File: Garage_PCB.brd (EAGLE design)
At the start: 35.6 x 44.4 mm, 19 parts, among them Q1 MOSFET-NCHANNELFQP30N06L

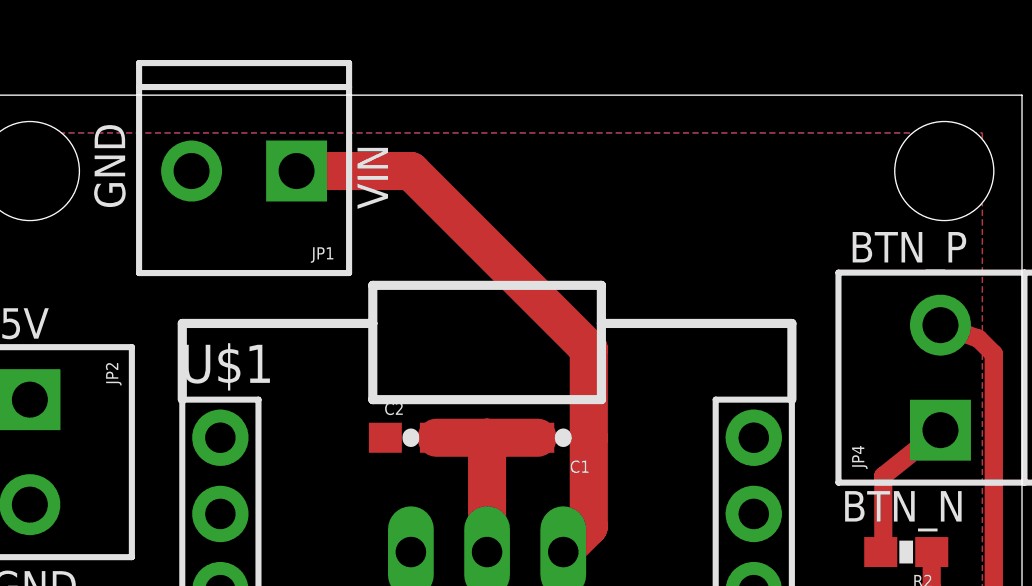
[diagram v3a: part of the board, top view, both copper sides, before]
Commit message: Added my name and the Spark logo
Added my name to the board and the Spark logo as well.  Also added the
Spark Eagle Library to the Eagle directory search paths so that I can
edit library parts.
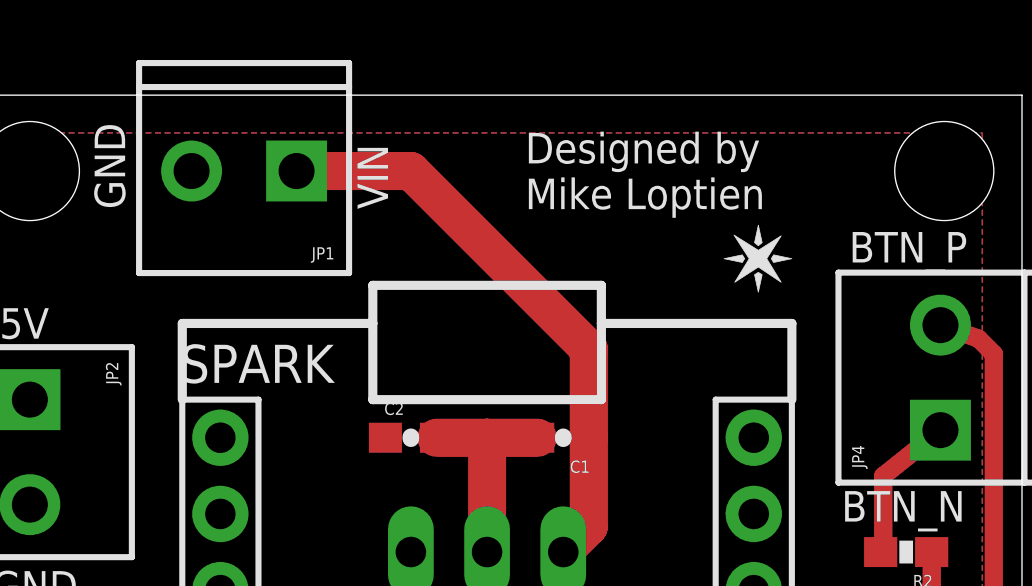
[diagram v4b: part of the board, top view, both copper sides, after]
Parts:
- added U$2: SPARK_LOGO2, Spark:SPARK_LOGO2
- renumbered U$1 to SPARK
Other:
- board text added: "Designed by Mike Loptien"
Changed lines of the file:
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@@
 <text x="1.27" y="25.781" size="1.016" layer="21" font="vector" ratio="15">RNG_I</text>
 <text x="1.27" y="16.891" size="1.016" layer="21" font="vector" ratio="15">LED_O</text>
+<text x="19.05" y="40.64" size="1.016" layer="21" font="vector" ratio="15">Designed by
+Mike Loptien</text>
 </plain>
 <attributes>
@@
 <elements>
 <element name="FRAME1" library="SparkFun-Aesthetics" package="CREATIVE_COMMONS" value="FRAME-LETTER" x="-77.47" y="49.53"/>
-<element name="U$1" library="Spark" package="SPARK_CORE" value="SPARK_CORECORE" x="17.78" y="19.05"/>
+<element name="SPARK" library="Spark" package="SPARK_CORE" value="SPARK_CORECORE" x="17.78" y="19.05"/>
 <element name="JP1" library="SparkFun-Connectors" package="SCREWTERMINAL-3.5MM-2" value="M023.5MM" x="11.43" y="41.91" rot="R180"/>
 <element name="JP2" library="SparkFun-Connectors" package="SCREWTERMINAL-3.5MM-2" value="M023.5MM" x="2.54" y="34.29" rot="R270"/>
@@
 <element name="STANDOFF4" library="SparkFun-Electromechanical" package="STAND-OFF" value="STAND-OFF" x="33.02" y="41.91"/>
 <element name="JP6" library="SparkFun-Connectors" package="SCREWTERMINAL-3.5MM-2" value="M023.5MM" x="2.54" y="23.495" rot="R270"/>
+<element name="U$2" library="Spark" package="SPARK_LOGO2" value="SPARK_LOGO2" x="25.654" y="40.132" smashed="yes" rot="R270"/>
 </elements>
 <signals>
 <signal name="VDDA">
-<contactref element="U$1" pad="22"/>
+<contactref element="SPARK" pad="22"/>
 </signal>
 <signal name="BTN_P">
@@
 <signal name="LED_O">
 <contactref element="JP3" pad="2"/>
-<contactref element="U$1" pad="17"/>
+<contactref element="SPARK" pad="17"/>
 <wire x1="2.54" y1="9.2" x2="2.54" y2="6.35" width="0.6096" layer="1"/>
 <wire x1="2.54" y1="6.35" x2="7.62" y2="1.27" width="0.6096" layer="1"/>
@@
 </signal>
 <signal name="3.3V">
-<contactref element="U$1" pad="24"/>
+<contactref element="SPARK" pad="24"/>
 </signal>
 <signal name="N$15">
-<contactref element="U$1" pad="19"/>
+<contactref element="SPARK" pad="19"/>
 <contactref element="R1" pad="1"/>
 <wire x1="30.9" y1="16.51" x2="30.9" y2="17.487" width="0.6096" layer="1"/>
@@
 </signal>
 <signal name="RNG_I">
-<contactref element="U$1" pad="6"/>
+<contactref element="SPARK" pad="6"/>
 <contactref element="JP3" pad="1"/>
 <wire x1="2.54" y1="12.7" x2="2.54" y2="13.97" width="0.6096" layer="1"/>
@@
 <contactref element="JP1" pad="2"/>
 <contactref element="JP2" pad="2"/>
-<contactref element="U$1" pad="2"/>
-<contactref element="U$1" pad="21"/>
+<contactref element="SPARK" pad="2"/>
+<contactref element="SPARK" pad="21"/>
 <polygon width="0.254" layer="16">
 <vertex x="1.27" y="43.18"/>
@@
 <contactref element="C2" pad="1"/>
 <contactref element="JP2" pad="1"/>
-<contactref element="U$1" pad="1"/>
+<contactref element="SPARK" pad="1"/>
 <contactref element="JP5" pad="1"/>
 <polygon width="0.254" layer="1" thermals="no">
@@
 </signal>
 <signal name="N$1">
-<contactref element="U$1" pad="16"/>
+<contactref element="SPARK" pad="16"/>
 <contactref element="R3" pad="1"/>
 <wire x1="26.67" y1="12.7" x2="29.122" y2="12.7" width="0.6096" layer="1"/>
@@
 <signal name="RNG2_I">
 <contactref element="JP6" pad="1"/>
-<contactref element="U$1" pad="5"/>
+<contactref element="SPARK" pad="5"/>
 <wire x1="8.89" y1="22.86" x2="8.255" y2="23.495" width="0.6096" layer="1"/>
 <wire x1="8.255" y1="23.495" x2="2.54" y2="23.495" width="0.6096" layer="1"/>
 </signal>
 <signal name="LED2_O">
-<contactref element="U$1" pad="18"/>
+<contactref element="SPARK" pad="18"/>
 <contactref element="JP6" pad="2"/>
 <wire x1="2.54" y1="19.995" x2="6.35" y2="16.51" width="0.6096" layer="16"/>
@@
 </board>
 </drawing>
+<compatibility>
+<note version="6.3" minversion="6.2.2" severity="warning">
+Since Version 6.2.2 text objects can contain more than one line,
+which will not be processed correctly with this version.
+</note>
+</compatibility>
 </eagle>

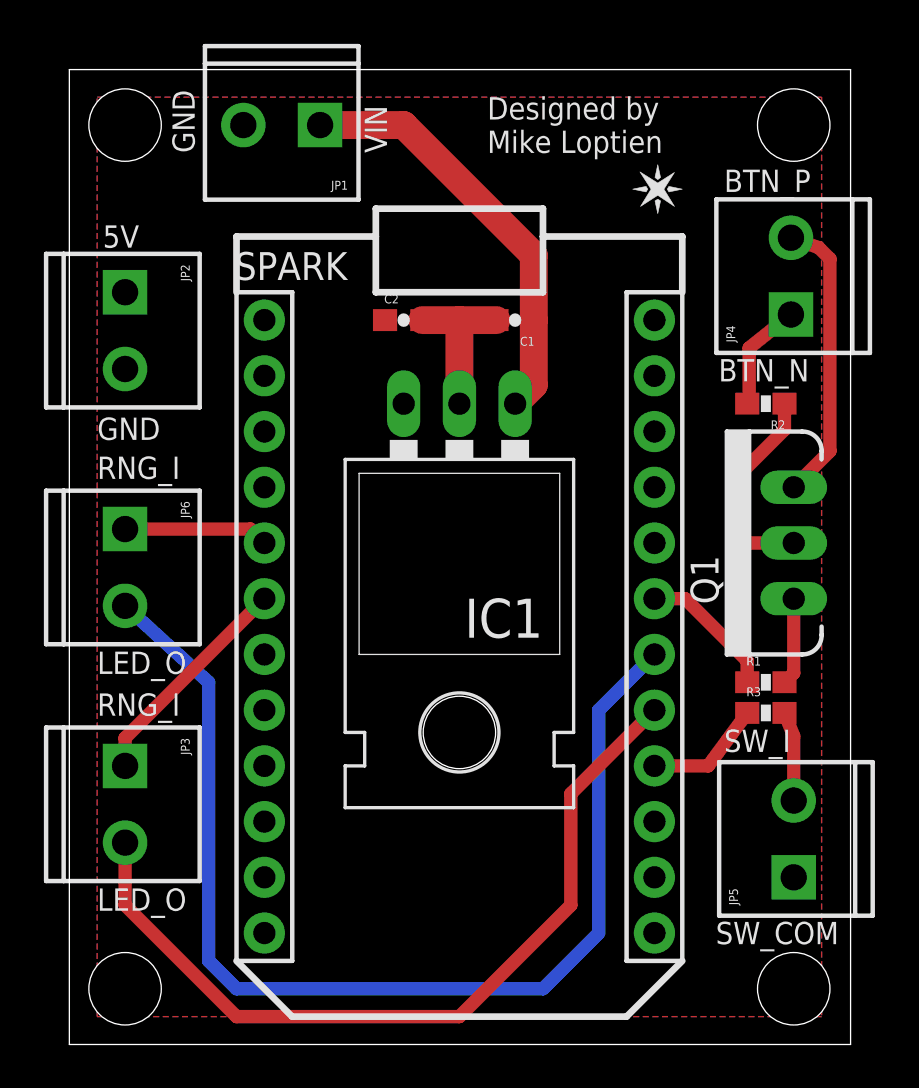
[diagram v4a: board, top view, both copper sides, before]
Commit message: Moved Mosfet and shrunk design
Moved the MOSFET underneath the Spark on the bottom layer so I can save
some space.  I moved just about everything around and was able to shrink
the board down to basically just the size of the Spark and the extra
width of the screw terminals.  It is very small now and costs almost $4
less to build.
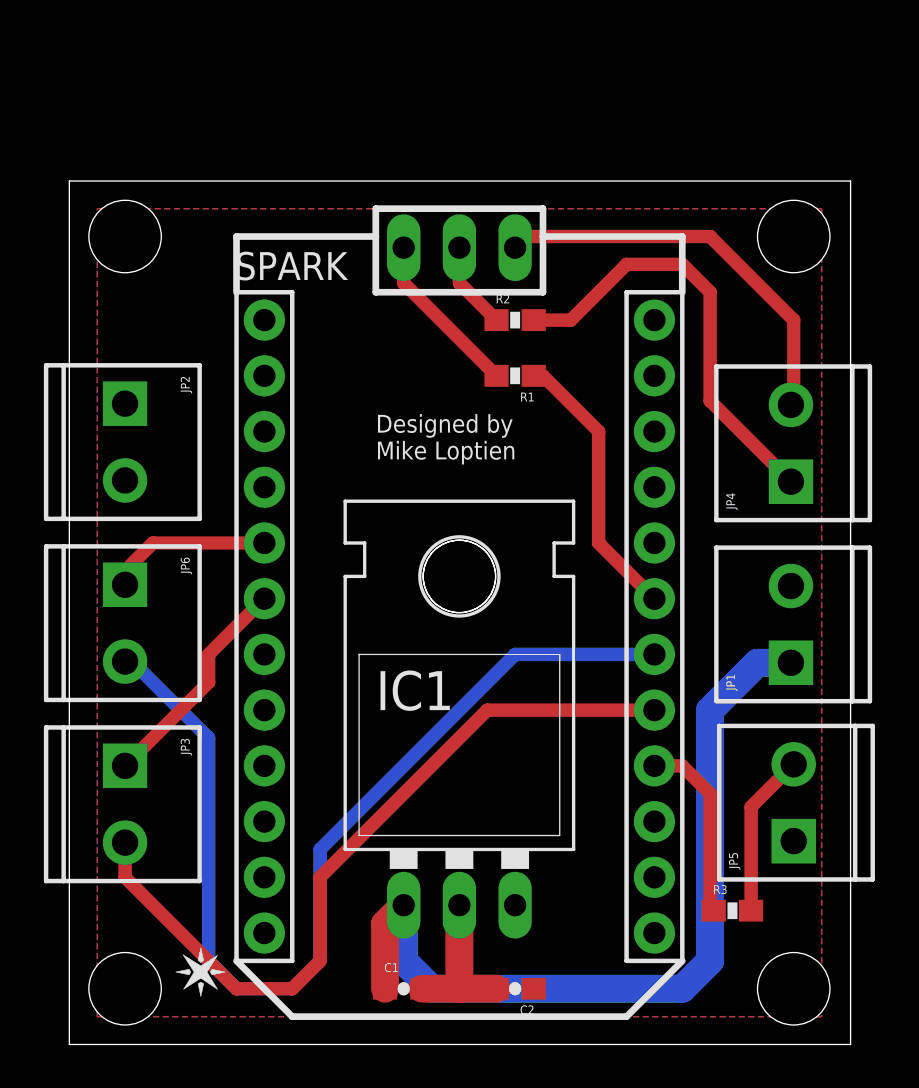
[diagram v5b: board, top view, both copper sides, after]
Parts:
- Q1: value MOSFET-NCHANNELFQP30N06L -> MOSFET-NCHANNELFQP30N06L-ALT; device SparkFun-DiscreteSemi:TO220V -> SparkFun-DiscreteSemi:TO220-ALT
- moved U$2 41.3 mm to (4.83, 4.45)
- moved JP1 32.6 mm to (32.9, 17.4), turned to 90 degrees
- moved C1 30.9 mm to (15.2, 2.54), turned to 0 degrees
- moved C2 30.9 mm to (20.3, 2.54), turned to 180 degrees
- moved R1 18.1 mm to (20.3, 30.5), turned to 180 degrees
- moved Q1 18.0 mm to (17.8, 32.5), flipped to the bottom, turned to 180 degrees
- moved IC1 15.2 mm to (17.8, 10.2), turned to 0 degrees
- moved R2 12.0 mm to (20.3, 33.0), turned to 0 degrees
- moved R3 9.14 mm to (30.2, 6.10)
- moved JP4 7.62 mm to (32.9, 25.7)
- moved JP2 5.08 mm to (2.54, 29.2)
- moved STANDOFF3 5.08 mm to (2.54, 36.8)
- moved STANDOFF4 5.08 mm to (33.0, 36.8)
- moved JP6 2.54 mm to (2.54, 21.0)
- moved JP5 1.65 mm to (33.0, 9.27)
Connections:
- net BTN_P renamed BTN_H
- removed net BTN_N: JP4.2, Q1.3
- new net BTN_L: JP4.2, Q1.OUT
- net N$16: now also Q1.IN; no longer Q1.1
- net N$17: now also Q1.GND; no longer Q1.2
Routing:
- net 24V: track 19.3 -> 37.7 mm
- net BTN_L: track 0.00 -> 18.4 mm
- net BTN_H: track 5.02 -> 19.8 mm
- net BTN_N: track 13.2 -> 0.00 mm
- net N$15: track 6.38 -> 12.7 mm
- net N$17: track 9.65 -> 4.00 mm
- net LED2_O: track 51.0 -> 45.5 mm
- net N$16: track 3.98 -> 7.59 mm
- net RD_SW_I: track 4.07 -> 7.48 mm
- net N$1: track 5.45 -> 8.47 mm
- net LED_O: track 37.8 -> 35.3 mm
- net RNG2_I: track 6.61 -> 7.51 mm
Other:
- board size 35.6 x 44.4 mm -> 35.6 x 39.4 mm

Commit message: Moved the Mosfet to top layer
Moved the Mosfet to the top layer and made the necessary changes to the
board to connect it.  Also moved one of the Range finder pins to be
closer to the other.  Added a thermal pad to the Mosfet and added some
thermal vias.
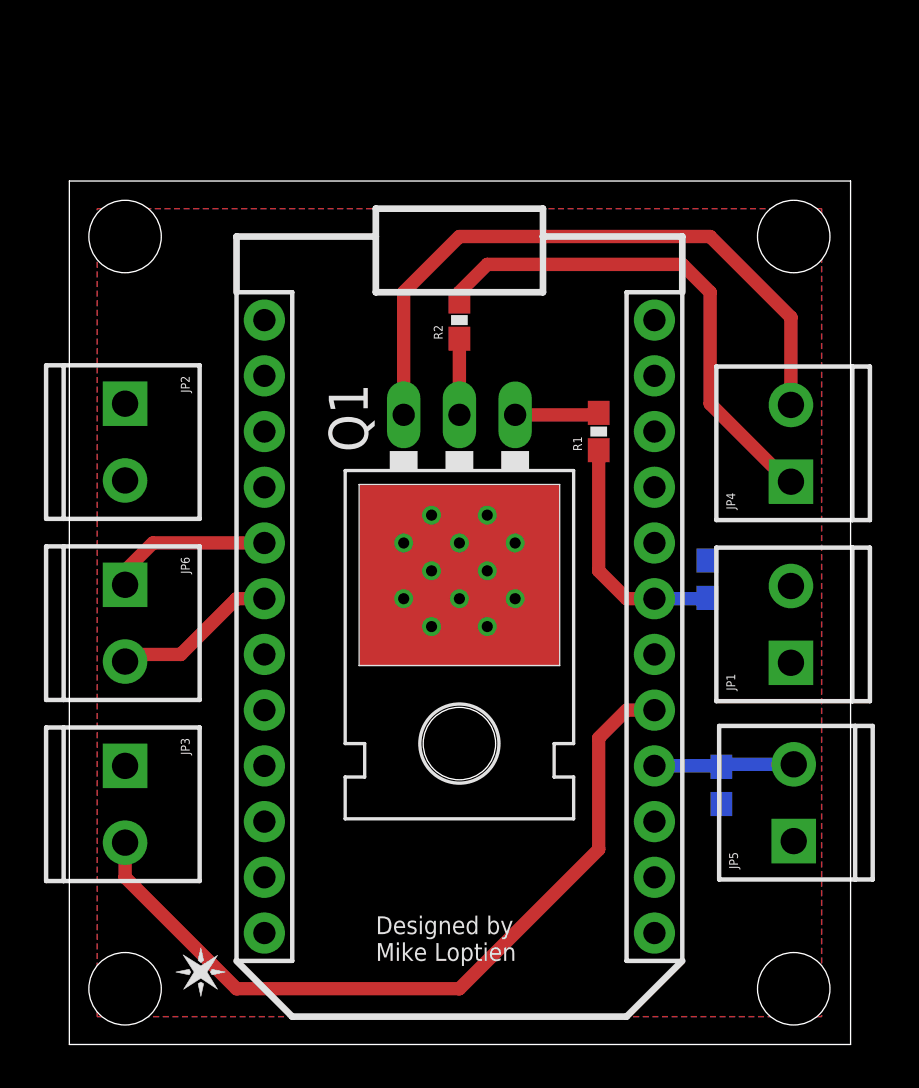
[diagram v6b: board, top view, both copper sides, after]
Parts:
- removed C1, C2: (no value), SparkFun-Capacitors:0603-CAP
- removed IC1: (no value), SparkFun-PowerIC:TO-220-ALT
- added FRAME2: FRAME-LETTER, SparkFun-Aesthetics:CREATIVE_COMMONS
- added R4: 10K, SparkFun-Resistors:0603-RES
- Q1: value MOSFET-NCHANNELFQP30N06L-ALT -> MOSFET-NCHANNEL_THRMTO-220-THRM; device SparkFun-DiscreteSemi:TO220-ALT -> SparkFun-DiscreteSemi:TO220-THRM
- R1: value 10K -> 66
- R3: value (none) -> 10K
- moved Q1 10.2 mm to (17.8, 22.4), flipped to the top
- moved R3 5.74 mm to (29.7, 11.8), flipped to the bottom, turned to 90 degrees
- moved R1 4.58 mm to (24.1, 27.9), turned to 90 degrees
- moved R2 2.54 mm to (17.8, 33.0), turned to 90 degrees
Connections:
- removed net 24V: C1.1, IC1.IN, JP1.1
- removed net LED2_O: JP6.2, SPARK.18
- removed net N$1: R3.1, SPARK.16
- net 5V: now also JP1.1, JP3.1; no longer C2.1, IC1.OUT
- net GND: now also Q1.THRM, R3.1, R4.1; no longer C1.2, C2.2, IC1.GND
- net N$15: now also R4.2
- net RD_SW_I: now also SPARK.16
- net RNG_I: now also JP6.2; no longer JP3.1
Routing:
- net LED2_O: track 45.5 -> 0.00 mm
- net 24V: track 37.7 -> 0.00 mm
- net GND: track 7.19 -> 27.5 mm, vias 0 -> 12
- net BTN_L: track 18.4 -> 29.8 mm
- net N$1: track 8.47 -> 0.00 mm
- net N$16: track 7.59 -> 3.85 mm
- net BTN_H: track 19.8 -> 23.1 mm
- net RNG_I: track 10.3 -> 7.54 mm
- net N$15: track 12.7 -> 11.0 mm
- net RD_SW_I: track 7.48 -> 6.41 mm
- net LED_O: track 35.3 -> 36.1 mm
- net N$17: track 4.00 -> 3.47 mm
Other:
- board text added: "SW_NO"
- board text removed: "SW_I"
- board text removed: "VIN"

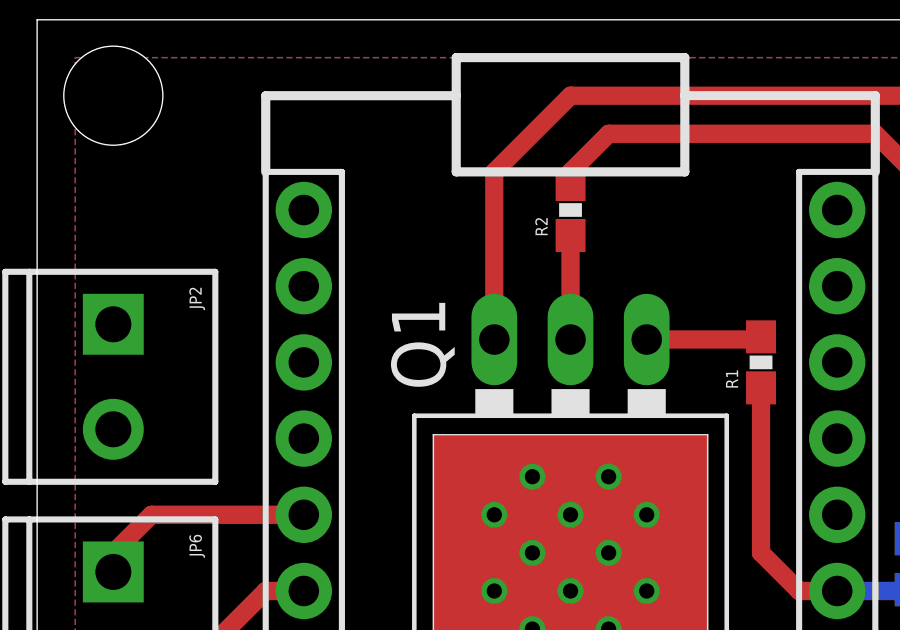
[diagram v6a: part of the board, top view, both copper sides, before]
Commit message: Added a pulldown to the BTN_L side
After some breadboard testing I found that the low side of the garage
door button needs to be pulled down to ground in order to de-energize
the line so that a new contact successfully gets registered.  Added this
pulldown and ordered this revision of the board.
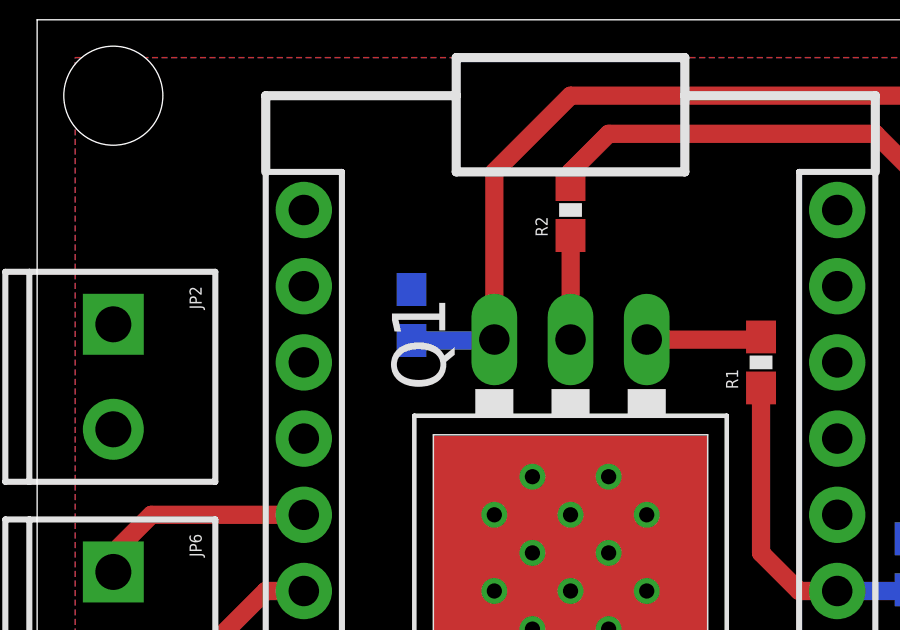
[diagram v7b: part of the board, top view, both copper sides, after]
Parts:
- added R5: 10K, SparkFun-Resistors:0603-RES
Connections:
- net BTN_L: now also R5.2
- net GND: now also R5.1
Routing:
- net BTN_L: track 29.8 -> 32.6 mm
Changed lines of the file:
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@@
 <setting verticaltext="up"/>
 </settings>
-<grid distance="0.05" unitdist="inch" unit="inch" style="lines" multiple="1" display="yes" altdistance="0.005" altunitdist="inch" altunit="inch"/>
+<grid distance="1" unitdist="mm" unit="mm" style="lines" multiple="1" display="yes" altdistance="0.1" altunitdist="mm" altunit="mm"/>
 <layers>
 <layer number="1" name="Top" color="4" fill="1" visible="yes" active="yes"/>
@@
 <layer number="23" name="tOrigins" color="15" fill="1" visible="yes" active="yes"/>
 <layer number="24" name="bOrigins" color="15" fill="1" visible="yes" active="yes"/>
-<layer number="25" name="tNames" color="7" fill="1" visible="yes" active="yes"/>
-<layer number="26" name="bNames" color="7" fill="1" visible="yes" active="yes"/>
+<layer number="25" name="tNames" color="7" fill="1" visible="no" active="yes"/>
+<layer number="26" name="bNames" color="7" fill="1" visible="no" active="yes"/>
 <layer number="27" name="tValues" color="7" fill="1" visible="no" active="yes"/>
 <layer number="28" name="bValues" color="7" fill="1" visible="no" active="yes"/>
@@
 <element name="FRAME2" library="SparkFun-Aesthetics" package="CREATIVE_COMMONS" value="FRAME-LETTER" x="-77.47" y="-12.7"/>
 <element name="JP1" library="SparkFun-Connectors" package="SCREWTERMINAL-3.5MM-2" value="M023.5MM" x="32.893" y="17.399" rot="R90"/>
+<element name="R5" library="SparkFun-Resistors" package="0603-RES" value="10K" x="12.48" y="29.52" rot="MR270"/>
 </elements>
 <signals>
@@
 <via x="16.51" y="19.05" extent="1-16" drill="0.508" shape="square"/>
 <wire x1="16.51" y1="19.05" x2="15.24" y2="17.78" width="0.6096" layer="1"/>
+<contactref element="R5" pad="1"/>
 </signal>
 <signal name="5V">
@@
 <wire x1="17.78" y1="36.83" x2="15.24" y2="34.29" width="0.6096" layer="1"/>
 <wire x1="15.24" y1="34.29" x2="15.24" y2="28.702" width="0.6096" layer="1"/>
+<contactref element="R5" pad="2"/>
+<wire x1="12.48" y1="28.67" x2="15.208" y2="28.67" width="0.6096" layer="16"/>
+<wire x1="15.208" y1="28.67" x2="15.24" y2="28.702" width="0.6096" layer="16"/>
 </signal>
 </signals>
